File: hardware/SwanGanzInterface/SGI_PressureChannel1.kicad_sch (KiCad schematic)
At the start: 14 parts, among them U4 INA122D, U5 OPA2350

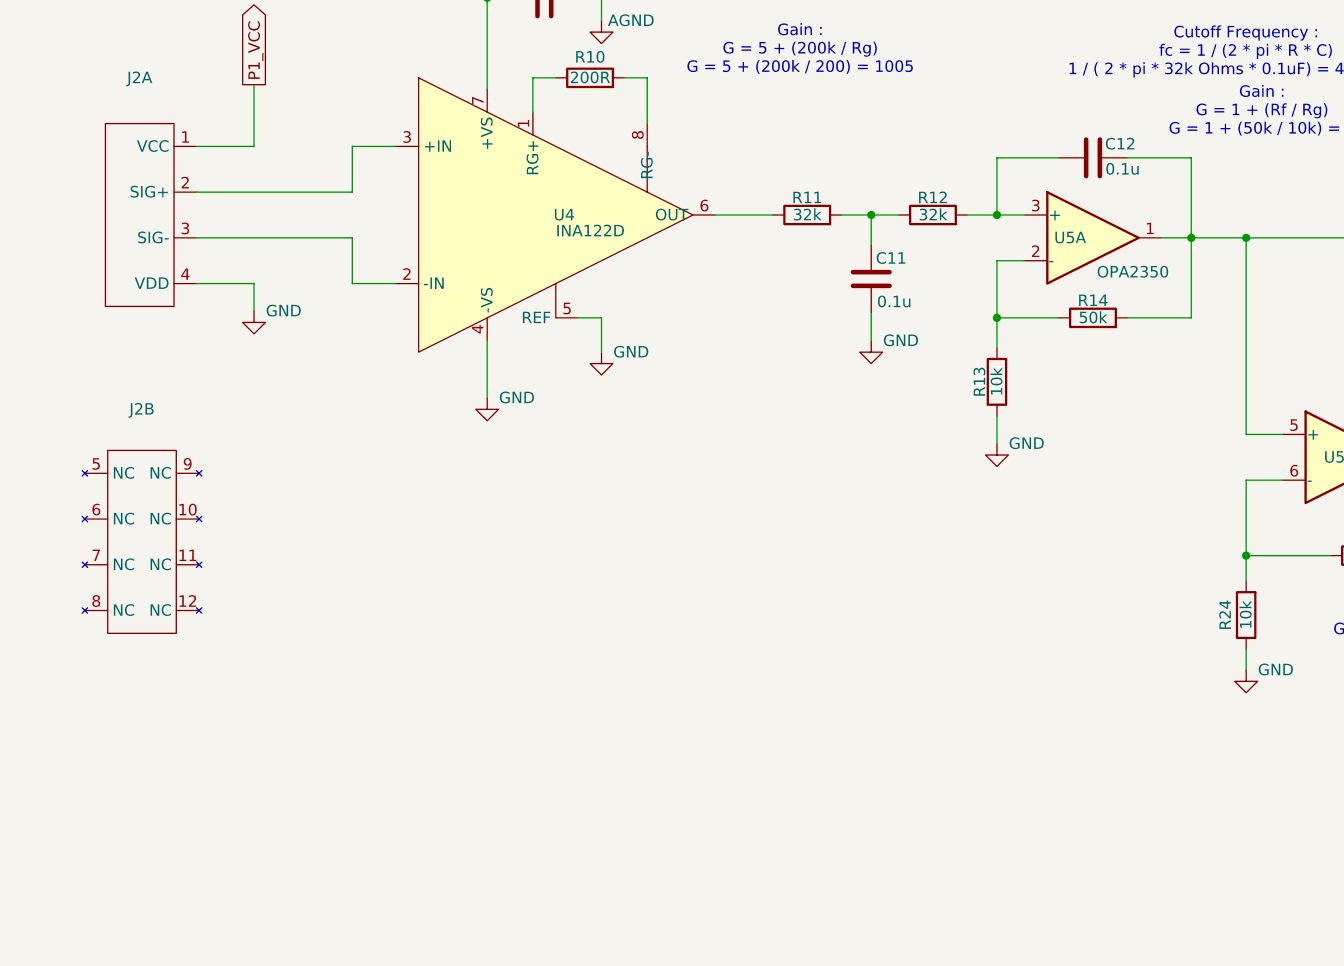
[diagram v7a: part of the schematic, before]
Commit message: Added launchpad, power jumpers, messed with symbol lib
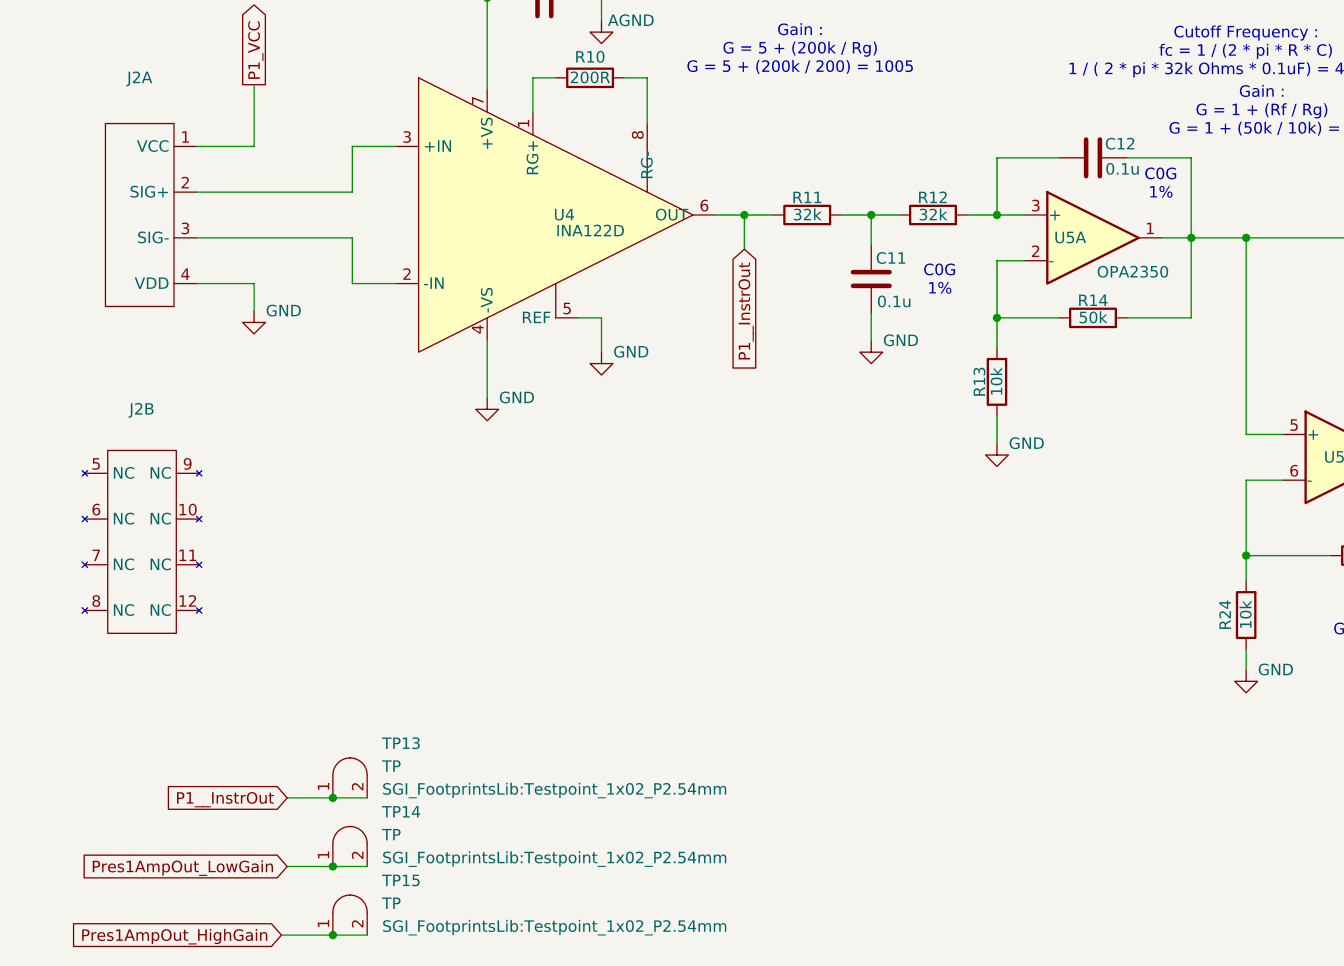
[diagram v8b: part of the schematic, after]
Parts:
- added TP13, TP14, TP15: TP, SGI_FootprintsLib:Testpoint_1x02_P2.54mm, symbol SGI_SymbolLib:Testpoint
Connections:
- net Pres1AmpOut_HighGain: now also TP15.1 (A), TP15.2 (B)
- net Pres1AmpOut_LowGain: now also TP14.1 (A), TP14.2 (B)
- net P1__InstrOut: now reaches R11.1, U4.6 (OUT)
- net P1__InstrOut: now also TP13.1 (A), TP13.2 (B)
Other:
- note added: "C0G 1%"
